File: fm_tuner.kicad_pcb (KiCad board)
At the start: 2 copper layers, 49 x 68.6 mm, 17 parts, among them IC1 ATMEGA328P-A, J1 ISP_Header, P2 USB_B, SW1 SW_PUSH, U1 16x2_LCD, U2 si4713_module

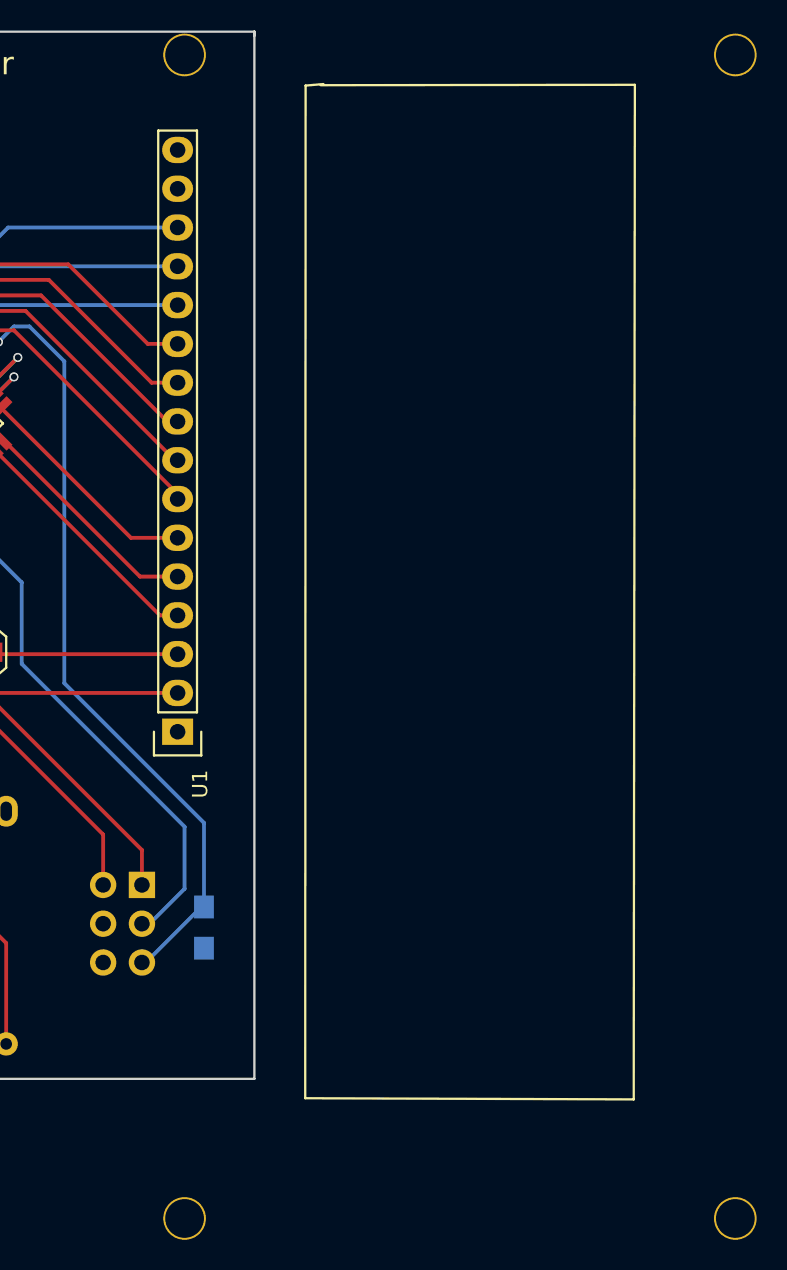
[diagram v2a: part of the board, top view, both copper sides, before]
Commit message: added a new footprint for LCD with no silkscreen outline of the screen replaced LCD footprint on board wiht new one changed pour clearance
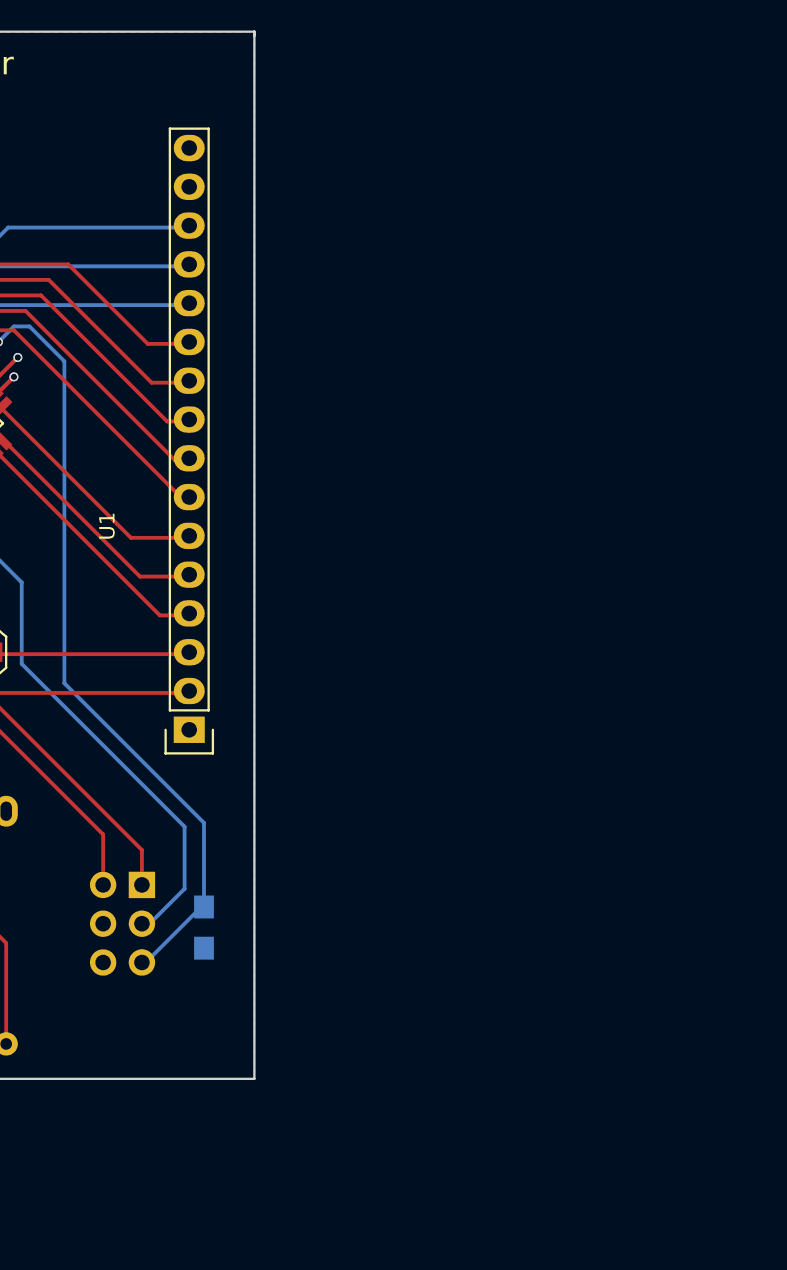
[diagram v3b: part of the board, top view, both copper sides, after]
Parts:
- U1: footprint fm_tuner:16x2_LCD -> fm_tuner:16x2_LCD_noscreen
- moved U1 30.3 mm to (59.7, 60.7)
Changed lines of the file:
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@@
   (general
     (links 57)
-    (no_connects 6)
-    (area -64.790201 13.132999 95.323 92.529)
+    (no_connects 1)
+    (area 13.132999 13.132999 62.305001 81.863001)
     (thickness 1.6)
     (drawings 8)
@@
   (layers
     (0 F.Cu signal)
-    (31 B.Cu signal)
+    (31 B.Cu signal hide)
     (32 B.Adhes user)
     (33 F.Adhes user)
@@
     (last_trace_width 0.25)
     (trace_clearance 0.2)
-    (zone_clearance 0.508)
+    (zone_clearance 0.3048)
     (zone_45_only no)
     (trace_min 0.2)
@@
       (net 2 VCC))
   )
-  (module fm_tuner:16x2_LCD (layer F.Cu)
-    (at 57.658 90.932 90)
-    (descr "16x2 LCD footprint qith 16 pins")
-    (tags "pin header")
-    (fp_text reference U1 (at 28.448 1.016 90) (layer F.SilkS)
-      (effects (font (size 1 1) (thickness 0.15)))
-    )
-    (fp_text value 16x2_LCD (at 31.877 -5.6896 90) (layer F.Fab) hide
-      (effects (font (size 1 1) (thickness 0.15)))
-    )
-    (fp_line (start 74.2188 8.9154) (end 74.2442 29.4894) (layer F.SilkS) (width 0.15))
-    (fp_line (start 74.2442 29.4894) (end 7.7978 29.4132) (layer F.SilkS) (width 0.15))
-    (fp_line (start 7.7978 29.4132) (end 7.874 7.8994) (layer F.SilkS) (width 0.15))
-    (fp_line (start 7.874 7.8994) (end 74.1934 7.9248) (layer F.SilkS) (width 0.15))
-    (fp_line (start 74.1934 7.9248) (end 74.295 9.0932) (layer F.SilkS) (width 0.15))
-    (fp_line (start 30.127 1.2928) (end 71.727 1.2928) (layer F.CrtYd) (width 0.05))
-    (fp_line (start 30.127 -2.2072) (end 71.727 -2.2072) (layer F.CrtYd) (width 0.05))
-    (fp_line (start 30.127 1.2928) (end 30.127 -2.2072) (layer F.CrtYd) (width 0.05))
-    (fp_line (start 71.727 1.2928) (end 71.727 -2.2072) (layer F.CrtYd) (width 0.05))
-    (fp_line (start 33.147 0.8128) (end 71.247 0.8128) (layer F.SilkS) (width 0.15))
-    (fp_line (start 71.247 0.8128) (end 71.247 -1.7272) (layer F.SilkS) (width 0.15))
-    (fp_line (start 71.247 -1.7272) (end 33.147 -1.7272) (layer F.SilkS) (width 0.15))
-    (fp_line (start 30.327 -2.0072) (end 31.877 -2.0072) (layer F.SilkS) (width 0.15))
-    (fp_line (start 33.147 -1.7272) (end 33.147 0.8128) (layer F.SilkS) (width 0.15))
-    (fp_line (start 31.877 1.0928) (end 30.327 1.0928) (layer F.SilkS) (width 0.15))
-    (fp_line (start 30.327 1.0928) (end 30.327 -2.0072) (layer F.SilkS) (width 0.15))
-    (pad 1 thru_hole rect (at 31.877 -0.4572 180) (size 2.032 1.7272) (drill 1.016) (layers *.Cu *.Mask F.SilkS)
-      (net 1 GND))
-    (pad 2 thru_hole oval (at 34.417 -0.4572 180) (size 2.032 1.7272) (drill 1.016) (layers *.Cu *.Mask F.SilkS)
-      (net 2 VCC))
-    (pad 3 thru_hole oval (at 36.957 -0.4572 180) (size 2.032 1.7272) (drill 1.016) (layers *.Cu *.Mask F.SilkS)
-      (net 30 "Net-(RV1-Pad2)"))
-    (pad 4 thru_hole oval (at 39.497 -0.4572 180) (size 2.032 1.7272) (drill 1.016) (layers *.Cu *.Mask F.SilkS)
-      (net 21 /RS))
-    (pad 5 thru_hole oval (at 42.037 -0.4572 180) (size 2.032 1.7272) (drill 1.016) (layers *.Cu *.Mask F.SilkS)
-      (net 22 /RW))
-    (pad 6 thru_hole oval (at 44.577 -0.4572 180) (size 2.032 1.7272) (drill 1.016) (layers *.Cu *.Mask F.SilkS)
-      (net 23 /EN))
-    (pad 7 thru_hole oval (at 47.117 -0.4572 180) (size 2.032 1.7272) (drill 1.016) (layers *.Cu *.Mask F.SilkS)
-      (net 27 "Net-(IC1-Pad30)"))
-    (pad 8 thru_hole oval (at 49.657 -0.4572 180) (size 2.032 1.7272) (drill 1.016) (layers *.Cu *.Mask F.SilkS)
-      (net 28 "Net-(IC1-Pad31)"))
-    (pad 9 thru_hole oval (at 52.197 -0.4572 180) (size 2.032 1.7272) (drill 1.016) (layers *.Cu *.Mask F.SilkS)
-      (net 29 "Net-(IC1-Pad32)"))
-    (pad 10 thru_hole oval (at 54.737 -0.4572 180) (size 2.032 1.7272) (drill 1.016) (layers *.Cu *.Mask F.SilkS)
-      (net 9 "Net-(IC1-Pad1)"))
-    (pad 11 thru_hole oval (at 57.277 -0.4572 180) (size 2.032 1.7272) (drill 1.016) (layers *.Cu *.Mask F.SilkS)
-      (net 10 "Net-(IC1-Pad2)"))
-    (pad 12 thru_hole oval (at 59.817 -0.4572 180) (size 2.032 1.7272) (drill 1.016) (layers *.Cu *.Mask F.SilkS)
-      (net 12 "Net-(IC1-Pad9)"))
-    (pad 13 thru_hole oval (at 62.357 -0.4572 180) (size 2.032 1.7272) (drill 1.016) (layers *.Cu *.Mask F.SilkS)
-      (net 13 "Net-(IC1-Pad10)"))
-    (pad 14 thru_hole oval (at 64.897 -0.4572 180) (size 2.032 1.7272) (drill 1.016) (layers *.Cu *.Mask F.SilkS)
-      (net 14 "Net-(IC1-Pad11)"))
-    (pad 15 thru_hole oval (at 67.437 -0.4572 180) (size 2.032 1.7272) (drill 1.016) (layers *.Cu *.Mask F.SilkS)
-      (net 31 "Net-(U1-Pad15)"))
-    (pad 16 thru_hole oval (at 69.977 -0.4572 180) (size 2.032 1.7272) (drill 1.016) (layers *.Cu *.Mask F.SilkS)
-      (net 32 "Net-(U1-Pad16)"))
-    (pad "" np_thru_hole circle (at 0 0 90) (size 2.794 2.794) (drill 2.54) (layers *.Cu *.Mask F.SilkS))
-    (pad "" np_thru_hole circle (at 76.2 0 90) (size 2.794 2.794) (drill 2.54) (layers *.Cu *.Mask F.SilkS))
-    (pad "" np_thru_hole circle (at 76.2 36.068 90) (size 2.794 2.794) (drill 2.54) (layers *.Cu *.Mask F.SilkS))
-    (pad "" np_thru_hole circle (at 0 36.068 90) (size 2.794 2.794) (drill 2.54) (layers *.Cu *.Mask F.SilkS))
-    (model Pin_Headers.3dshapes/Pin_Header_Straight_1x16.wrl
-      (at (xyz 0 -0.75 0))
-      (scale (xyz 1 1 1))
-      (rotate (xyz 0 0 90))
-    )
-  )
   (module Pin_Headers:Pin_Header_Straight_1x11 (layer F.Cu)
     (at 19.558 79.502 180)
@@
       (scale (xyz 1 1 1))
       (rotate (xyz 0 0 0))
+    )
+  )
+  (module fm_tuner:16x2_LCD_noscreen (layer F.Cu)
+    (at 59.69 60.706 90)
+    (descr "16x2 LCD footprint qith 16 pins")
+    (tags "pin header")
+    (fp_text reference U1 (at 15.113 -7.0866 90) (layer F.SilkS)
+      (effects (font (size 1 1) (thickness 0.15)))
+    )
+    (fp_text value 16x2_LCD (at 1.778 -6.9596 90) (layer F.Fab)
+      (effects (font (size 1 1) (thickness 0.15)))
+    )
+    (fp_line (start 0.028 0.0228) (end 41.628 0.0228) (layer F.CrtYd) (width 0.05))
+    (fp_line (start 0.028 -3.4772) (end 41.628 -3.4772) (layer F.CrtYd) (width 0.05))
+    (fp_line (start 0.028 0.0228) (end 0.028 -3.4772) (layer F.CrtYd) (width 0.05))
+    (fp_line (start 41.628 0.0228) (end 41.628 -3.4772) (layer F.CrtYd) (width 0.05))
+    (fp_line (start 3.048 -0.4572) (end 41.148 -0.4572) (layer F.SilkS) (width 0.15))
+    (fp_line (start 41.148 -0.4572) (end 41.148 -2.9972) (layer F.SilkS) (width 0.15))
+    (fp_line (start 41.148 -2.9972) (end 3.048 -2.9972) (layer F.SilkS) (width 0.15))
+    (fp_line (start 0.228 -3.2772) (end 1.778 -3.2772) (layer F.SilkS) (width 0.15))
+    (fp_line (start 3.048 -2.9972) (end 3.048 -0.4572) (layer F.SilkS) (width 0.15))
+    (fp_line (start 1.778 -0.1772) (end 0.228 -0.1772) (layer F.SilkS) (width 0.15))
+    (fp_line (start 0.228 -0.1772) (end 0.228 -3.2772) (layer F.SilkS) (width 0.15))
+    (pad 1 thru_hole rect (at 1.778 -1.7272 180) (size 2.032 1.7272) (drill 1.016) (layers *.Cu *.Mask F.SilkS)
+      (net 1 GND))
+    (pad 2 thru_hole oval (at 4.318 -1.7272 180) (size 2.032 1.7272) (drill 1.016) (layers *.Cu *.Mask F.SilkS)
+      (net 2 VCC))
+    (pad 3 thru_hole oval (at 6.858 -1.7272 180) (size 2.032 1.7272) (drill 1.016) (layers *.Cu *.Mask F.SilkS)
+      (net 30 "Net-(RV1-Pad2)"))
+    (pad 4 thru_hole oval (at 9.398 -1.7272 180) (size 2.032 1.7272) (drill 1.016) (layers *.Cu *.Mask F.SilkS)
+      (net 21 /RS))
+    (pad 5 thru_hole oval (at 11.938 -1.7272 180) (size 2.032 1.7272) (drill 1.016) (layers *.Cu *.Mask F.SilkS)
+      (net 22 /RW))
+    (pad 6 thru_hole oval (at 14.478 -1.7272 180) (size 2.032 1.7272) (drill 1.016) (layers *.Cu *.Mask F.SilkS)
+      (net 23 /EN))
+    (pad 7 thru_hole oval (at 17.018 -1.7272 180) (size 2.032 1.7272) (drill 1.016) (layers *.Cu *.Mask F.SilkS)
+      (net 27 "Net-(IC1-Pad30)"))
+    (pad 8 thru_hole oval (at 19.558 -1.7272 180) (size 2.032 1.7272) (drill 1.016) (layers *.Cu *.Mask F.SilkS)
+      (net 28 "Net-(IC1-Pad31)"))
+    (pad 9 thru_hole oval (at 22.098 -1.7272 180) (size 2.032 1.7272) (drill 1.016) (layers *.Cu *.Mask F.SilkS)
+      (net 29 "Net-(IC1-Pad32)"))
+    (pad 10 thru_hole oval (at 24.638 -1.7272 180) (size 2.032 1.7272) (drill 1.016) (layers *.Cu *.Mask F.SilkS)
+      (net 9 "Net-(IC1-Pad1)"))
+    (pad 11 thru_hole oval (at 27.178 -1.7272 180) (size 2.032 1.7272) (drill 1.016) (layers *.Cu *.Mask F.SilkS)
+      (net 10 "Net-(IC1-Pad2)"))
+    (pad 12 thru_hole oval (at 29.718 -1.7272 180) (size 2.032 1.7272) (drill 1.016) (layers *.Cu *.Mask F.SilkS)
+      (net 12 "Net-(IC1-Pad9)"))
+    (pad 13 thru_hole oval (at 32.258 -1.7272 180) (size 2.032 1.7272) (drill 1.016) (layers *.Cu *.Mask F.SilkS)
+      (net 13 "Net-(IC1-Pad10)"))
+    (pad 14 thru_hole oval (at 34.798 -1.7272 180) (size 2.032 1.7272) (drill 1.016) (layers *.Cu *.Mask F.SilkS)
+      (net 14 "Net-(IC1-Pad11)"))
+    (pad 15 thru_hole oval (at 37.338 -1.7272 180) (size 2.032 1.7272) (drill 1.016) (layers *.Cu *.Mask F.SilkS)
+      (net 31 "Net-(U1-Pad15)"))
+    (pad 16 thru_hole oval (at 39.878 -1.7272 180) (size 2.032 1.7272) (drill 1.016) (layers *.Cu *.Mask F.SilkS)
+      (net 32 "Net-(U1-Pad16)"))
+    (model Pin_Headers.3dshapes/Pin_Header_Straight_1x16.wrl
+      (at (xyz 0 -0.75 0))
+      (scale (xyz 1 1 1))
+      (rotate (xyz 0 0 90))
     )
   )
@@
   (segment (start 20.03298 18.796) (end 19.77898 19.05) (width 0.25) (layer F.Cu) (net 43))
   (zone (net 1) (net_name GND) (layer F.Cu) (hatch edge 0.508)
-    (connect_pads (clearance 0.508))
+    (connect_pads (clearance 0.3048))
     (min_thickness 0.254)
     (fill yes (arc_segments 16) (thermal_gap 0.508) (thermal_bridge_width 0.508))
